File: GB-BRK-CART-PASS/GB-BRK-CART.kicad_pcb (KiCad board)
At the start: 2 copper layers, 63.5 x 102 mm, 97 parts, among them J1 Conn_02x16_Odd_Even, J2 DNF, J3 GameBoy_Cartridge

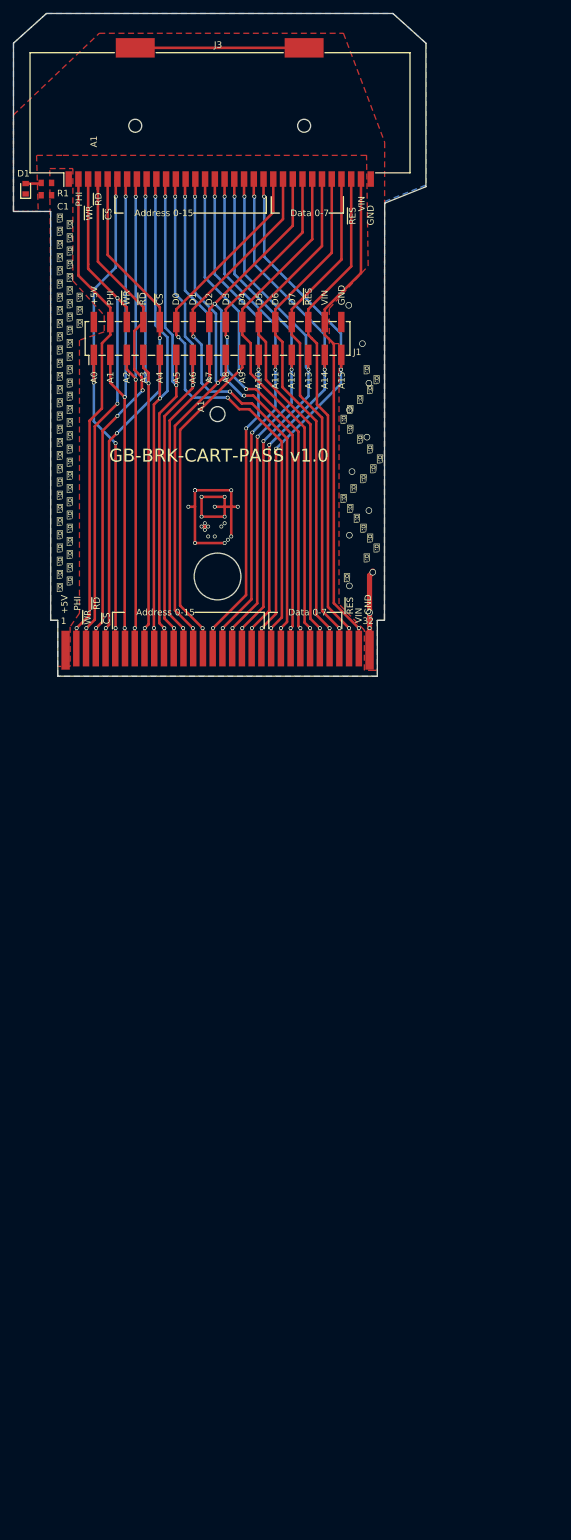
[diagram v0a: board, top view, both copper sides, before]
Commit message: Update passthrough cart to 2.0
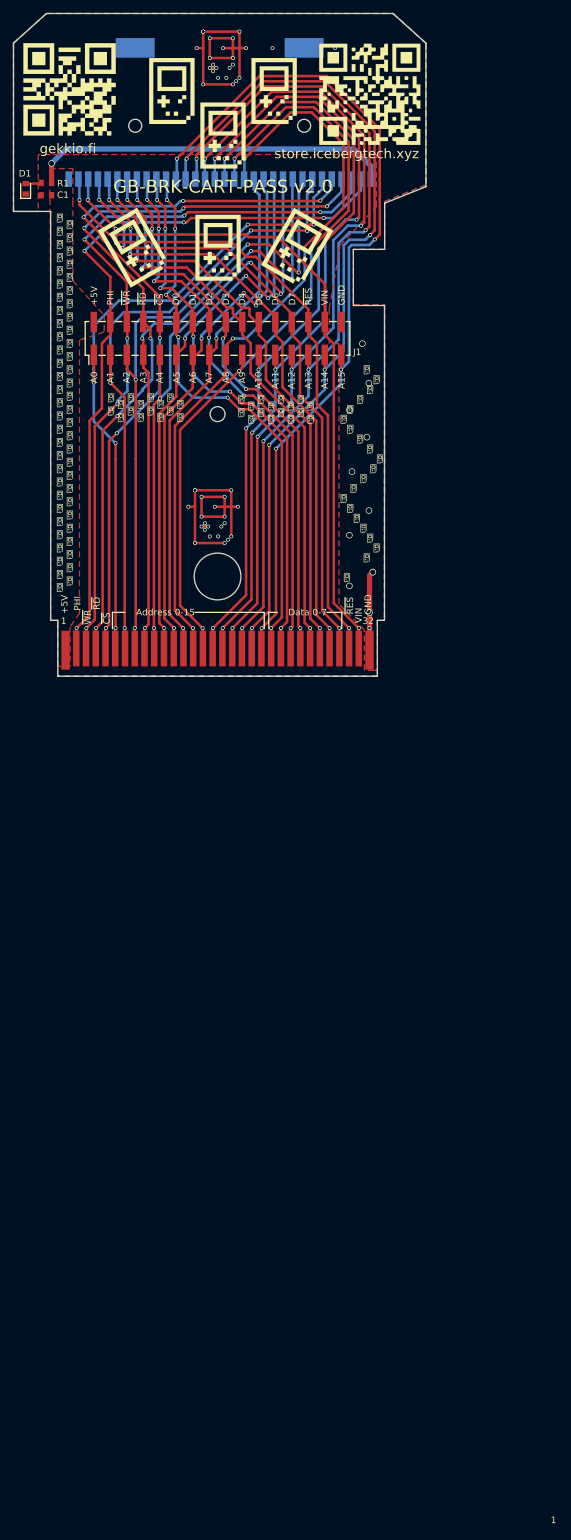
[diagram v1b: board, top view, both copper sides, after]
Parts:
- removed the G*** at (88.9, 5.08)
- removed the G*** at (126.5, 14.2)
- removed the G*** at (78.7, 41.7)
- removed the G*** at (78.7, 43.7)
- removed the G*** at (78.7, 45.7)
- removed the G*** at (119.1, 9.65)
- removed the G*** at (100.3, 22.4)
- added ?: , , F.Cu at (66.3, 111.8)
- added ?: , , F.Cu at (72.9, 95.8)
- added ?: , , F.Cu at (85.3, 117.9)
- added ?: , , F.Cu at (76.5, 91.9)
- added ?: , , F.Cu at (119.4, 96.3)
- added ?: , , F.Cu at (128.8, 87.4)
- added G***: LOGO, SilkScreen:gb-icon-ss, B.Cu at (107.4, 39.4)
- added G***: LOGO, SilkScreen:gb-icon-ss, B.Cu at (110.5, 39.4)
- added G***: LOGO, SilkScreen:gb-icon-ss, B.Cu at (118.1, 38.4)
- added G***: LOGO, SilkScreen:gb-icon-ss, B.Cu at (113.5, 37.3)
- added G***: LOGO, SilkScreen:gb-icon-ss, B.Cu at (115.1, 36.3)
- added G***: LOGO, SilkScreen:gb-icon-ss, B.Cu at (113.5, 39.4)
- added G***: LOGO, SilkScreen:gb-icon-ss, B.Cu at (116.6, 39.4)
- added G***: LOGO, SilkScreen:gb-icon-ss, B.Cu at (112.0, 38.4)
- added G***: LOGO, SilkScreen:gb-icon-ss, B.Cu at (95.2, 39.4)
- added G***: LOGO, SilkScreen:gb-icon-ss, B.Cu at (96.8, 36.3)
- added G***: LOGO, SilkScreen:gb-icon-ss, B.Cu at (95.2, 37.3)
- added G***: LOGO, SilkScreen:gb-icon-ss, B.Cu at (109.0, 36.3)
- added G***: LOGO, SilkScreen:gb-icon-ss, B.Cu at (102.9, 38.4)
- added G***: LOGO, SilkScreen:gb-icon-ss, B.Cu at (105.9, 36.3)
- added G***: LOGO, SilkScreen:gb-icon-ss, B.Cu at (96.8, 38.4)
- added G***: LOGO, SilkScreen:gb-icon-ss, B.Cu at (99.8, 36.3)
- added G***: LOGO, SilkScreen:gb-icon-ss, B.Cu at (104.4, 37.3)
- added G***: LOGO, SilkScreen:gb-icon-ss, B.Cu at (98.3, 37.3)
- added G***: LOGO, SilkScreen:gb-icon-ss, B.Cu at (98.3, 39.4)
- added G***: LOGO, SilkScreen:gb-icon-ss, B.Cu at (105.9, 38.4)
- added G***: LOGO, SilkScreen:gb-icon-ss, B.Cu at (101.3, 37.3)
- added G***: LOGO, SilkScreen:gb-icon-ss, B.Cu at (102.9, 36.3)
- added G***: LOGO, SilkScreen:gb-icon-ss, B.Cu at (107.4, 37.3)
- added G***: LOGO, SilkScreen:gb-icon-ss, B.Cu at (101.3, 39.4)
- added G***: LOGO, SilkScreen:gb-icon-ss, B.Cu at (104.4, 39.4)
- added G***: LOGO, SilkScreen:gb-icon-ss, B.Cu at (99.8, 38.4)
- added G***: LOGO, SilkScreen:gb-icon-ss, B.Cu at (83.3, 39.1)
- added G***: LOGO, SilkScreen:gb-icon-ss, B.Cu at (84.8, 36.1)
- added G***: LOGO, SilkScreen:gb-icon-ss, B.Cu at (83.3, 37.1)
- added G***: LOGO, SilkScreen:gb-icon-ss, B.Cu at (90.9, 38.1)
- added G***: LOGO, SilkScreen:gb-icon-ss, B.Cu at (94.0, 36.1)
- added G***: LOGO, SilkScreen:gb-icon-ss, B.Cu at (84.8, 38.1)
- added G***: LOGO, SilkScreen:gb-icon-ss, B.Cu at (87.9, 36.1)
- added G***: LOGO, SilkScreen:gb-icon-ss, B.Cu at (115.1, 38.4)
- added G***: LOGO, SilkScreen:gb-icon-ss, B.Cu at (92.5, 37.1)
- added G***: LOGO, SilkScreen:gb-icon-ss, B.Cu at (86.4, 37.1)
- added G***: LOGO, SilkScreen:gb-icon-ss, B.Cu at (86.4, 39.1)
- added G***: LOGO, SilkScreen:gb-icon-ss, B.Cu at (94.0, 38.1)
- added G***: LOGO, SilkScreen:gb-icon-ss, B.Cu at (89.4, 37.1)
- added G***: LOGO, SilkScreen:gb-icon-ss, B.Cu at (90.9, 36.1)
- added G***: LOGO, SilkScreen:gb-icon-ss, B.Cu at (89.4, 39.1)
- added G***: LOGO, SilkScreen:gb-icon-ss, B.Cu at (92.5, 39.1)
- added G***: LOGO, SilkScreen:gb-icon-ss, B.Cu at (87.9, 38.1)
- added G***: LOGO, SilkScreen:gb-icon-ss, F.Cu at (114.3, 60.5)
- added G***: LOGO, SilkScreen:gb-icon-ss, B.Cu at (118.1, 36.3)
- added G***: LOGO, SilkScreen:gb-icon-ss, F.Cu at (112.8, 57.4)
- added G***: LOGO, SilkScreen:gb-icon-ss, F.Cu at (114.3, 58.4)
- added G***: LOGO, SilkScreen:gb-icon-ss, F.Cu at (106.7, 59.4)
- added G***: LOGO, SilkScreen:gb-icon-ss, F.Cu at (103.6, 57.4)
- added G***: LOGO, SilkScreen:gb-icon-ss, F.Cu at (112.8, 59.4)
- added G***: LOGO, SilkScreen:gb-icon-ss, F.Cu at (109.7, 57.4)
- added G***: LOGO, SilkScreen:gb-icon-ss, F.Cu at (105.2, 58.4)
- added G***: LOGO, SilkScreen:gb-icon-ss, F.Cu at (111.3, 58.4)
- added G***: LOGO, SilkScreen:gb-icon-ss, F.Cu at (111.3, 60.5)
- added G***: LOGO, SilkScreen:gb-icon-ss, F.Cu at (103.6, 59.4)
- added G***: LOGO, SilkScreen:gb-icon-ss, B.Cu at (109.0, 38.4)
- added G***: LOGO, SilkScreen:gb-icon-ss, F.Cu at (108.2, 58.4)
- added G***: LOGO, SilkScreen:gb-icon-ss, F.Cu at (106.7, 57.4)
- added G***: LOGO, SilkScreen:gb-icon-ss, F.Cu at (108.2, 60.5)
- added G***: LOGO, SilkScreen:gb-icon-ss, F.Cu at (105.2, 60.5)
- added G***: LOGO, SilkScreen:gb-icon-ss, F.Cu at (109.7, 59.4)
- added G***: LOGO, SilkScreen:gb-icon-ss, F.Cu at (94.2, 60.2)
- added G***: LOGO, SilkScreen:gb-icon-ss, F.Cu at (92.7, 57.1)
- added G***: LOGO, SilkScreen:gb-icon-ss, F.Cu at (94.2, 58.2)
- added G***: LOGO, SilkScreen:gb-icon-ss, F.Cu at (86.6, 59.2)
- added G***: LOGO, SilkScreen:gb-icon-ss, F.Cu at (83.6, 57.1)
- added G***: LOGO, SilkScreen:gb-icon-ss, B.Cu at (112.0, 36.3)
- added G***: LOGO, SilkScreen:gb-icon-ss, F.Cu at (92.7, 59.2)
- added G***: LOGO, SilkScreen:gb-icon-ss, F.Cu at (89.7, 57.1)
- added G***: LOGO, SilkScreen:gb-icon-ss, F.Cu at (85.1, 58.2)
- added G***: LOGO, SilkScreen:gb-icon-ss, F.Cu at (91.2, 58.2)
- added G***: LOGO, SilkScreen:gb-icon-ss, F.Cu at (91.2, 60.2)
- added G***: LOGO, SilkScreen:gb-icon-ss, F.Cu at (83.6, 59.2)
- added G***: LOGO, SilkScreen:gb-icon-ss, F.Cu at (88.1, 58.2)
- added G***: LOGO, SilkScreen:gb-icon-ss, F.Cu at (86.6, 57.1)
- added G***: LOGO, SilkScreen:gb-icon-ss, F.Cu at (88.1, 60.2)
- added G***: LOGO, SilkScreen:gb-icon-ss, F.Cu at (85.1, 60.2)
- added G***: LOGO, SilkScreen:gb-icon-ss, B.Cu at (116.6, 37.3)
- added G***: LOGO, SilkScreen:gb-icon-ss, F.Cu at (89.7, 59.2)
- added G***: LOGO, SilkScreen:gb-icon-400dpi, F.Cu at (87.1, 34.0)
- added G***: LOGO, SilkScreen:qr-shop.icebergtech.xyz, F.Cu at (123.4, 10.4)
- added G***: LOGO, SilkScreen:gb-icon-400dpi, F.Cu at (100.1, 34.0)
- added G***: LOGO, SilkScreen:gb-icon-400dpi, F.Cu at (100.8, 16.8)
- added G***: LOGO, SilkScreen:gb-icon-ss, B.Cu at (110.5, 37.3)
- G*** (x4): moved to F.Cu
- J3: moved to B.Cu
- moved G*** 64.5 mm to (77.2, 9.65), turned to 0 degrees
- moved G*** 29.0 mm to (112.3, 34.0), turned to 330 degrees
- moved G*** 27.2 mm to (108.7, 9.91), turned to 0 degrees
- moved G*** 19.3 mm to (93.0, 9.91), turned to 0 degrees
- turned J3 to 180 degrees
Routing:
- net +5V: track 0.00 -> 56.1 mm, vias 0 -> 1
- net /A15: track 84.6 -> 135.8 mm, vias 4 -> 5
- net Net-(J1-Pad29): track 83.8 -> 131.6 mm, vias 4 -> 5
- net /A13: track 82.9 -> 128.8 mm, vias 4 -> 5
- net (no net): track 45.2 -> 90.4 mm, vias 22 -> 44
- net /A12: track 82.0 -> 125.6 mm, vias 4 -> 5
- net /A11: track 81.2 -> 122.5 mm, vias 4 -> 5
- net /~CS: track 79.1 -> 117.6 mm, vias 3 -> 6
- net /A10: track 80.3 -> 118.7 mm, vias 4 -> 5
- net /A9: track 82.4 -> 119.1 mm, vias 3 -> 4
- net /PHI: track 76.5 -> 113.2 mm, vias 1 -> 4
- net /~RD: track 81.1 -> 116.5 mm, vias 3 -> 6
- net /~WR: track 80.4 -> 114.5 mm, vias 3 -> 6
- net /A8: track 82.5 -> 114.1 mm, vias 3 -> 4
- net /VIN: track 76.8 -> 105.2 mm, vias 1 -> 2
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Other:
- outline, holes or cut-outs redrawn
- board text added: "Based on GB-BRK-CART v4.0 https://github.com/Gekkio/gb-hardware"
- board text added: "GB-BRK-CART-PASS v2.0"
- board text added: "JLCJLCJLCJLC"
- board text added: "Source https://github.com/ice-bergtech/gb-hardware"
- board text added: "gekkio.fi"
- board text added: "store.icebergtech.xyz"
- board text removed: "GB-BRK-CART-PASS v1.0"
- board text removed: "https://gekkio.fi"
- board text removed: "https://store.icebergtech.xyz"
